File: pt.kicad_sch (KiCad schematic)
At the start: 7 parts, among them J6 PT

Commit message: new BOM
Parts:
- C39: Part # Generic 100nF 6.3V X7R 0402 MLCC -> Generic CAP CER 0.1UF 6.3V X7R 0402
- D22: value BZV55-B5V1 -> 5.1V; Manufacturer Nexperia -> Nexperia USA Inc.
- R72: Part # Generic 1K 1% 0402 Resistor -> Generic RES SMD 1K OHM 1% 1/16W 0402
- R73: Part # Generic 5K 1% 0402 Resistor -> Generic RES SMD 5K OHM 0.1% 1/16W 0402
- R74: Part # Generic 10K 1% 0402 Resistor -> Generic RES SMD 10K OHM 1% 1/4W 0402
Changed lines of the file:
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@@
 			)
 		)
-		(property "Value" "BZV55-B5V1"
+		(property "Value" "5.1V"
 			(at 132.08 99.695 90)
 			(effects
@@
 			)
 		)
-		(property "Manufacturer" "Nexperia"
+		(property "Manufacturer" "Nexperia USA Inc."
 			(at 129.54 97.79 0)
 			(effects
@@
 			)
 		)
-		(property "Manufacturer" "~"
+		(property "Manufacturer" ""
 			(at 102.87 92.71 0)
 			(effects
@@
 			)
 		)
-		(property "Part #" "~"
+		(property "Part #" ""
 			(at 102.87 92.71 0)
 			(effects
@@
 			)
 		)
-		(property "Part #" "Generic 1K 1% 0402 Resistor"
+		(property "Part #" "Generic RES SMD 1K OHM 1% 1/16W 0402"
 			(at 124.46 92.71 0)
 			(effects
@@
 			)
 		)
-		(property "Part #" "Generic 10K 1% 0402 Resistor"
+		(property "Part #" "Generic RES SMD 10K OHM 1% 1/4W 0402"
 			(at 173.99 109.22 0)
 			(effects
@@
 			)
 		)
-		(property "Part #" "Generic 100nF 6.3V X7R 0402 MLCC"
+		(property "Part #" "Generic CAP CER 0.1UF 6.3V X7R 0402"
 			(at 143.51 81.28 0)
 			(effects
@@
 			)
 		)
-		(property "Part #" "Generic 5K 1% 0402 Resistor"
+		(property "Part #" "Generic RES SMD 5K OHM 0.1% 1/16W 0402"
 			(at 173.99 99.06 0)
 			(effects

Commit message: Added power sense to rocket2-battery with voltage follower, added +1 solenoids and PT circuit, made new gx connectors
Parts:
- J6: footprint Connector_PinHeader_2.54mm:PinHeader_1x03_P2.54mm_Vertical -> 0UCIRP-KiCAD-Lib:GX-12 3 pin
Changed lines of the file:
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@@
+					(unit 1)
+				)
+				(path "/02606b2c-b376-4ffb-9781-f9cea3f70994/beec90aa-dde0-4584-822f-65a1d5b7e933"
+					(reference "#PWR090")
 					(unit 1)
 				)
@@
 					(unit 1)
 				)
+				(path "/02606b2c-b376-4ffb-9781-f9cea3f70994/beec90aa-dde0-4584-822f-65a1d5b7e933"
+					(reference "D11")
+					(unit 1)
+				)
 				(path "/02606b2c-b376-4ffb-9781-f9cea3f70994/d17f7a69-0b50-4135-8e0c-909f4988d142"
 					(reference "D22")
@@
 			)
 		)
-		(property "Footprint" "Connector_PinHeader_2.54mm:PinHeader_1x03_P2.54mm_Vertical"
+		(property "Footprint" "0UCIRP-KiCAD-Lib:GX-12 3 pin"
 			(at 102.87 92.71 0)
 			(effects
@@
 				(path "/02606b2c-b376-4ffb-9781-f9cea3f70994/bb7a760b-2886-469d-8bee-376c1221151c"
 					(reference "J19")
+					(unit 1)
+				)
+				(path "/02606b2c-b376-4ffb-9781-f9cea3f70994/beec90aa-dde0-4584-822f-65a1d5b7e933"
+					(reference "J14")
 					(unit 1)
 				)
@@
 					(unit 1)
 				)
+				(path "/02606b2c-b376-4ffb-9781-f9cea3f70994/beec90aa-dde0-4584-822f-65a1d5b7e933"
+					(reference "#PWR0365")
+					(unit 1)
+				)
 				(path "/02606b2c-b376-4ffb-9781-f9cea3f70994/d17f7a69-0b50-4135-8e0c-909f4988d142"
 					(reference "#PWR0104")
@@
 				(path "/02606b2c-b376-4ffb-9781-f9cea3f70994/bb7a760b-2886-469d-8bee-376c1221151c"
 					(reference "R113")
+					(unit 1)
+				)
+				(path "/02606b2c-b376-4ffb-9781-f9cea3f70994/beec90aa-dde0-4584-822f-65a1d5b7e933"
+					(reference "R6")
 					(unit 1)
 				)
@@
 					(unit 1)
 				)
+				(path "/02606b2c-b376-4ffb-9781-f9cea3f70994/beec90aa-dde0-4584-822f-65a1d5b7e933"
+					(reference "R8")
+					(unit 1)
+				)
 				(path "/02606b2c-b376-4ffb-9781-f9cea3f70994/d17f7a69-0b50-4135-8e0c-909f4988d142"
 					(reference "R74")
@@
 				(path "/02606b2c-b376-4ffb-9781-f9cea3f70994/bb7a760b-2886-469d-8bee-376c1221151c"
 					(reference "#PWR0282")
+					(unit 1)
+				)
+				(path "/02606b2c-b376-4ffb-9781-f9cea3f70994/beec90aa-dde0-4584-822f-65a1d5b7e933"
+					(reference "#PWR094")
 					(unit 1)
 				)
@@
 					(unit 1)
 				)
+				(path "/02606b2c-b376-4ffb-9781-f9cea3f70994/beec90aa-dde0-4584-822f-65a1d5b7e933"
+					(reference "#PWR092")
+					(unit 1)
+				)
 				(path "/02606b2c-b376-4ffb-9781-f9cea3f70994/d17f7a69-0b50-4135-8e0c-909f4988d142"
 					(reference "#PWR0100")
@@
 					(unit 1)
 				)
+				(path "/02606b2c-b376-4ffb-9781-f9cea3f70994/beec90aa-dde0-4584-822f-65a1d5b7e933"
+					(reference "#PWR096")
+					(unit 1)
+				)
 				(path "/02606b2c-b376-4ffb-9781-f9cea3f70994/d17f7a69-0b50-4135-8e0c-909f4988d142"
 					(reference "#PWR0102")
@@
 					(unit 1)
 				)
+				(path "/02606b2c-b376-4ffb-9781-f9cea3f70994/beec90aa-dde0-4584-822f-65a1d5b7e933"
+					(reference "#PWR0367")
+					(unit 1)
+				)
 				(path "/02606b2c-b376-4ffb-9781-f9cea3f70994/d17f7a69-0b50-4135-8e0c-909f4988d142"
 					(reference "#PWR0106")
@@
 					(unit 1)
 				)
+				(path "/02606b2c-b376-4ffb-9781-f9cea3f70994/beec90aa-dde0-4584-822f-65a1d5b7e933"
+					(reference "C7")
+					(unit 1)
+				)
 				(path "/02606b2c-b376-4ffb-9781-f9cea3f70994/d17f7a69-0b50-4135-8e0c-909f4988d142"
 					(reference "C39")
@@
 					(unit 1)
 				)
+				(path "/02606b2c-b376-4ffb-9781-f9cea3f70994/beec90aa-dde0-4584-822f-65a1d5b7e933"
+					(reference "#PWR098")
+					(unit 1)
+				)
 				(path "/02606b2c-b376-4ffb-9781-f9cea3f70994/d17f7a69-0b50-4135-8e0c-909f4988d142"
 					(reference "#PWR0103")
@@
 					(unit 1)
 				)
+				(path "/02606b2c-b376-4ffb-9781-f9cea3f70994/beec90aa-dde0-4584-822f-65a1d5b7e933"
+					(reference "R7")
+					(unit 1)
+				)
 				(path "/02606b2c-b376-4ffb-9781-f9cea3f70994/d17f7a69-0b50-4135-8e0c-909f4988d142"
 					(reference "R73")
@@
 					(unit 1)
 				)
+				(path "/02606b2c-b376-4ffb-9781-f9cea3f70994/beec90aa-dde0-4584-822f-65a1d5b7e933"
+					(reference "U5")
+					(unit 1)
+				)
 				(path "/02606b2c-b376-4ffb-9781-f9cea3f70994/d17f7a69-0b50-4135-8e0c-909f4988d142"
 					(reference "U28")
@@
 					(unit 1)
 				)
+				(path "/02606b2c-b376-4ffb-9781-f9cea3f70994/beec90aa-dde0-4584-822f-65a1d5b7e933"
+					(reference "#PWR0366")
+					(unit 1)
+				)

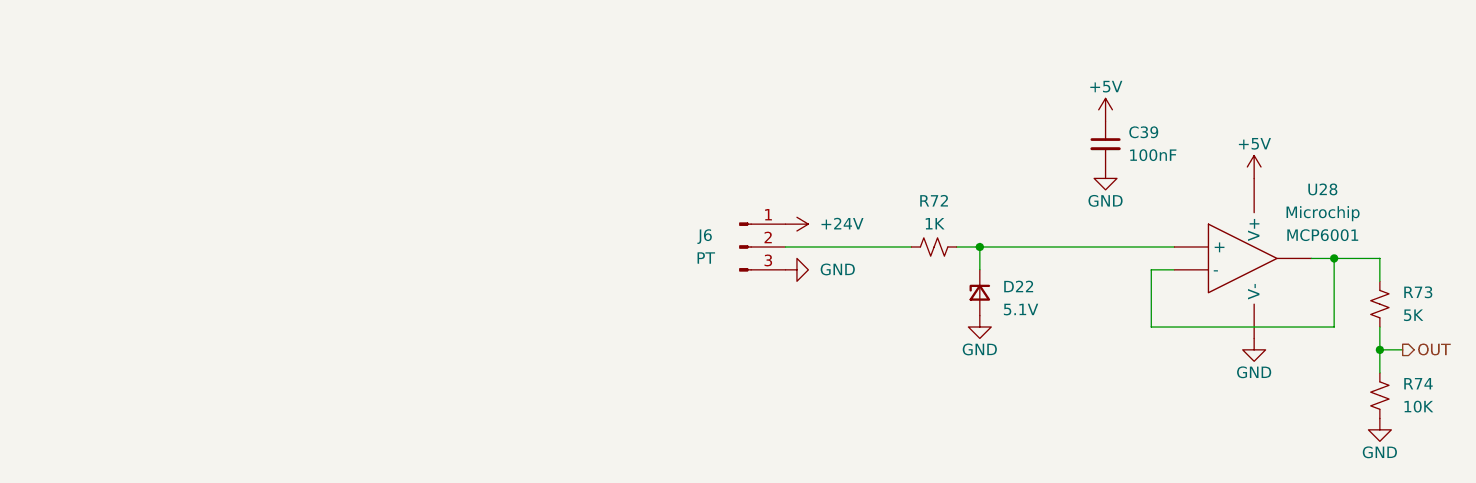
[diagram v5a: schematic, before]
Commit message: Deleted 5V, edited LPFs on TCs and PTs
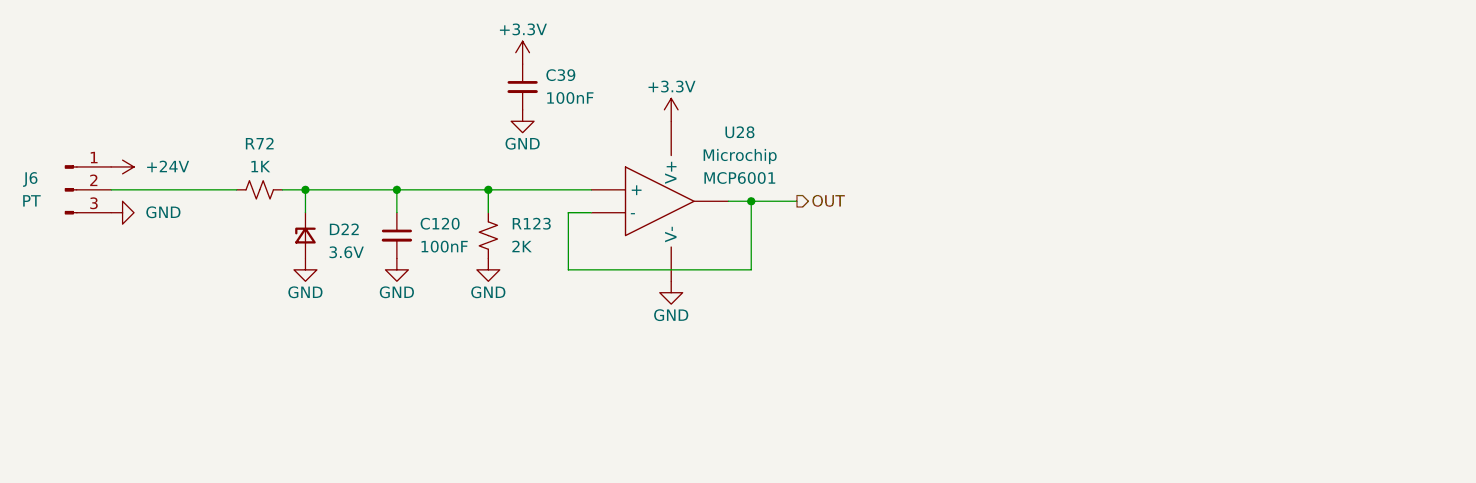
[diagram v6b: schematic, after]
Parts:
- removed R73: 5K, Resistor_SMD:R_0402_1005Metric, symbol Device:R_Small_US
- removed R74: 10K, Resistor_SMD:R_0402_1005Metric, symbol Device:R_Small_US
- added C120: 100nF, Capacitor_SMD:C_0402_1005Metric, symbol Device:C_Small
- added R123: 2K, Resistor_SMD:R_0402_1005Metric, symbol Device:R_Small_US
- D22: value 5.1V -> 3.6V; footprint Diode_SMD:D_MiniMELF -> Diode_SMD:D_SOD-882
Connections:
- net GND: now also C120.2, R123.1
- net OUT: now also U28.1, U28.4 (-)
- net at D22.1 (K), R72.2, U28.3 (+): now also C120.1, R123.2
- net +5V renamed +3.3V
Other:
- moved on the sheet: C39, D22, J6, R72, U28

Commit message: version in PCBway 12/12/2025
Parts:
- J6: now not fitted
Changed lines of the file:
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@@
 		(in_bom yes)
 		(on_board yes)
-		(dnp no)
+		(dnp yes)
 		(property "Reference" "J6"
 			(at 24.13 85.09 0)

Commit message: added some production files
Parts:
- D22: value 3.6V -> 3.9V; Manufacturer Nexperia USA Inc. -> Diodes Incorporated; Part # BZV55-B5V1 -> BZT52C3V9LP-7
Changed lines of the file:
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@@
 			)
 		)
-		(property "Value" "3.6V"
+		(property "Value" "3.9V"
 			(at 57.15 93.345 90)
 			(effects
@@
 			)
 		)
-		(property "Datasheet" "https://assets.nexperia.com/documents/data-sheet/BZV55_SER.pdf"
+		(property "Datasheet" "https://mm.digikey.com/Volume0/opasdata/d220001/medias/docus/4849/DS_31_BZT52C2V4LP-BZT52C39LP.pdf"
 			(at 54.61 91.44 90)
 			(effects
@@
 			)
 		)
-		(property "Manufacturer" "Nexperia USA Inc."
+		(property "Manufacturer" "  Diodes Incorporated"
 			(at 54.61 91.44 0)
 			(effects
@@
 			)
 		)
-		(property "Part #" "BZV55-B5V1"
+		(property "Part #" " BZT52C3V9LP-7"
 			(at 54.61 91.44 0)
 			(effects
